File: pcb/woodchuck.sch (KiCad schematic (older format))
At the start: 5 parts, among them IC1 ADP3335, P1 CONN_01X02

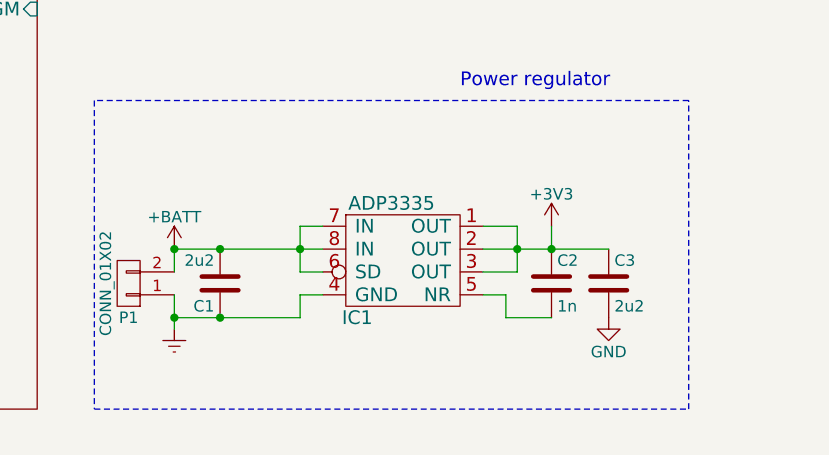
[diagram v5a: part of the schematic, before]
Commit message: Assigned a few footprints. Still need to find out if it is possible to hide all footprint names from the schematics.
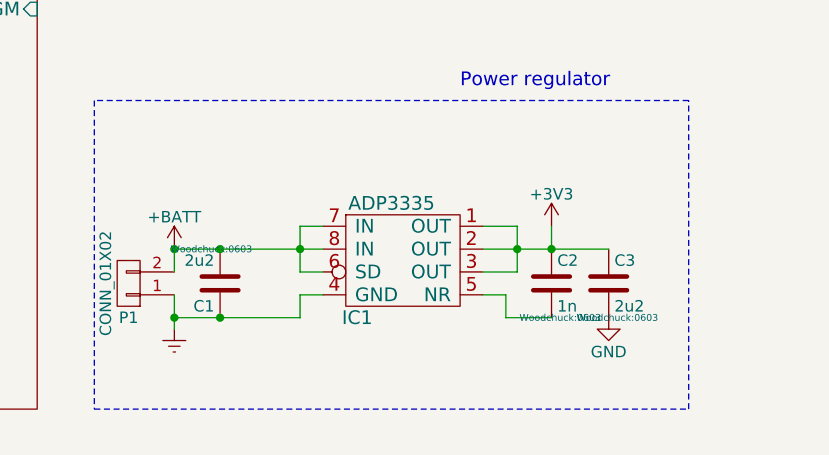
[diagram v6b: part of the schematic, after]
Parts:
- C1, C2, C3: footprint (none) -> Woodchuck:0603
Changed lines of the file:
@@
 F 0 "C2" H 5875 6800 50  0000 L CNN
 F 1 "1n" H 5875 6600 50  0000 L CNN
-F 2 "" H 5888 6550 30  0000 C CNN
+F 2 "Woodchuck:0603" H 5888 6550 30  0000 C CNN
 F 3 "" H 5850 6700 60  0000 C CNN
 	1    5850 6700
@@
 F 0 "C3" H 6125 6800 50  0000 L CNN
 F 1 "2u2" H 6125 6600 50  0000 L CNN
-F 2 "" H 6138 6550 30  0000 C CNN
+F 2 "Woodchuck:0603" H 6138 6550 30  0000 C CNN
 F 3 "" H 6100 6700 60  0000 C CNN
 	1    6100 6700
@@
 F 0 "C1" H 4425 6800 50  0000 L CNN
 F 1 "2u2" H 4425 6600 50  0000 L CNN
-F 2 "" H 4438 6550 30  0000 C CNN
+F 2 "Woodchuck:0603" H 4438 6550 30  0000 C CNN
 F 3 "" H 4400 6700 60  0000 C CNN
 	1    4400 6700

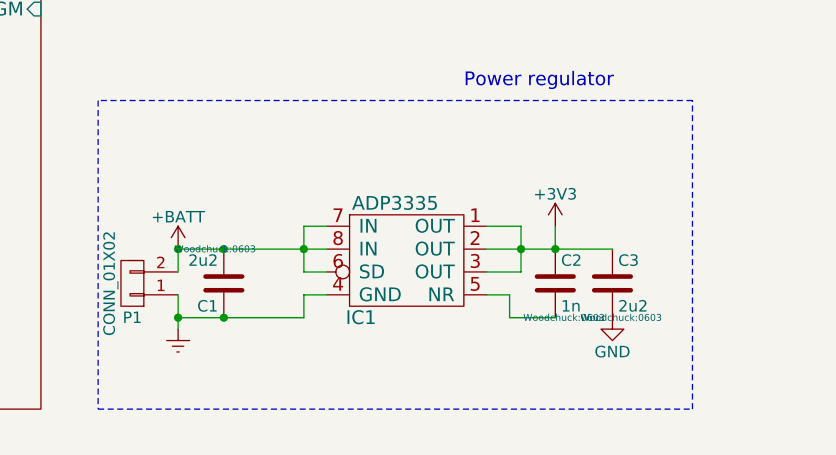
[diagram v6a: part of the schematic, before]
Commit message: Add some footprints
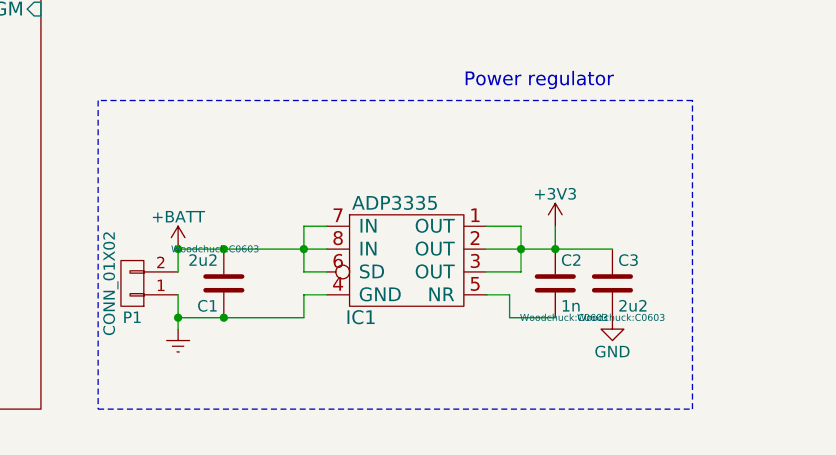
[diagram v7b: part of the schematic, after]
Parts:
- C1, C2, C3: footprint Woodchuck:0603 -> Woodchuck:C0603; Digikey (none) -> Value; Farnell (none) -> Value; Fieldname (none) -> Value
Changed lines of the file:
@@
 F 0 "C2" H 5875 6800 50  0000 L CNN
 F 1 "1n" H 5875 6600 50  0000 L CNN
-F 2 "Woodchuck:0603" H 5888 6550 30  0000 C CNN
+F 2 "Woodchuck:C0603" H 5888 6550 30  0000 C CNN
 F 3 "" H 5850 6700 60  0000 C CNN
+F 4 "Value" H 5850 6700 60  0001 C CNN "Digikey"
+F 5 "Value" H 5850 6700 60  0001 C CNN "Farnell"
+F 6 "Value" H 5850 6700 60  0001 C CNN "Fieldname"
 	1    5850 6700
 	1    0    0    -1
 $EndComp
 $Comp
-L Earth #PWR01
+L Earth #PWR2
 U 1 1 565E4C8C
 P 4200 6900
-F 0 "#PWR01" H 4200 6650 50  0001 C CNN
+F 0 "#PWR2" H 4200 6650 50  0001 C CNN
 F 1 "Earth" H 4200 6750 50  0001 C CNN
 F 2 "" H 4200 6900 60  0000 C CNN
@@
 F 0 "C3" H 6125 6800 50  0000 L CNN
 F 1 "2u2" H 6125 6600 50  0000 L CNN
-F 2 "Woodchuck:0603" H 6138 6550 30  0000 C CNN
+F 2 "Woodchuck:C0603" H 6138 6550 30  0000 C CNN
 F 3 "" H 6100 6700 60  0000 C CNN
+F 4 "Value" H 6100 6700 60  0001 C CNN "Digikey"
+F 5 "Value" H 6100 6700 60  0001 C CNN "Farnell"
+F 6 "Value" H 6100 6700 60  0001 C CNN "Fieldname"
 	1    6100 6700
 	1    0    0    -1
@@
 Connection ~ 4750 6550
 $Comp
-L GND #PWR02
+L GND #PWR4
 U 1 1 565E565A
 P 6100 6850
-F 0 "#PWR02" H 6100 6600 50  0001 C CNN
+F 0 "#PWR4" H 6100 6600 50  0001 C CNN
 F 1 "GND" H 6100 6700 50  0000 C CNN
 F 2 "" H 6100 6850 60  0000 C CNN
@@
 F 0 "C1" H 4425 6800 50  0000 L CNN
 F 1 "2u2" H 4425 6600 50  0000 L CNN
-F 2 "Woodchuck:0603" H 4438 6550 30  0000 C CNN
+F 2 "Woodchuck:C0603" H 4438 6550 30  0000 C CNN
 F 3 "" H 4400 6700 60  0000 C CNN
+F 4 "Value" H 4400 6700 60  0001 C CNN "Digikey"
+F 5 "Value" H 4400 6700 60  0001 C CNN "Farnell"
+F 6 "Value" H 4400 6700 60  0001 C CNN "Fieldname"
 	1    4400 6700
 	-1   0    0    1
@@
 	4200 6650 4200 6550
 $Comp
-L +BATT #PWR03
+L +BATT #PWR1
 U 1 1 565EBEEE
 P 4200 6550
-F 0 "#PWR03" H 4200 6400 50  0001 C CNN
+F 0 "#PWR1" H 4200 6400 50  0001 C CNN
 F 1 "+BATT" H 4200 6690 50  0000 C CNN
 F 2 "" H 4200 6550 60  0000 C CNN
@@
 Connection ~ 4200 6850
 $Comp
-L +3V3 #PWR04
+L +3V3 #PWR3
 U 1 1 565EC163
 P 5850 6450
-F 0 "#PWR04" H 5850 6300 50  0001 C CNN
+F 0 "#PWR3" H 5850 6300 50  0001 C CNN
 F 1 "+3V3" H 5850 6590 50  0000 C CNN
 F 2 "" H 5850 6450 60  0000 C CNN
